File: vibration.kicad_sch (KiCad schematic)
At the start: 7 parts, among them J5 Conn_01x02, Q3 SS8050

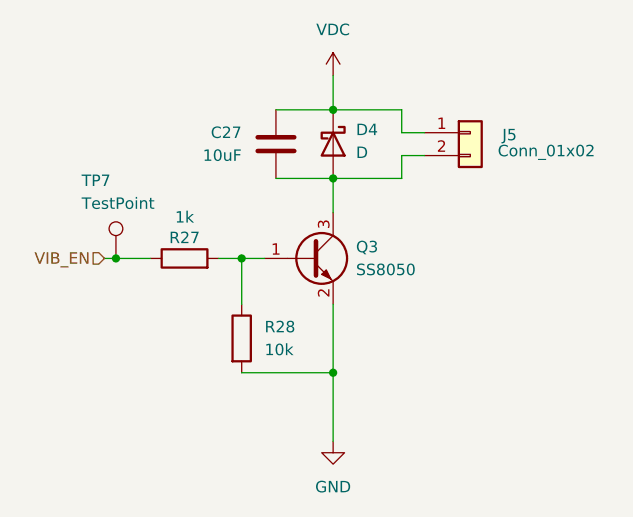
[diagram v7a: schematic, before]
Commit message: proper lcd backlight driver
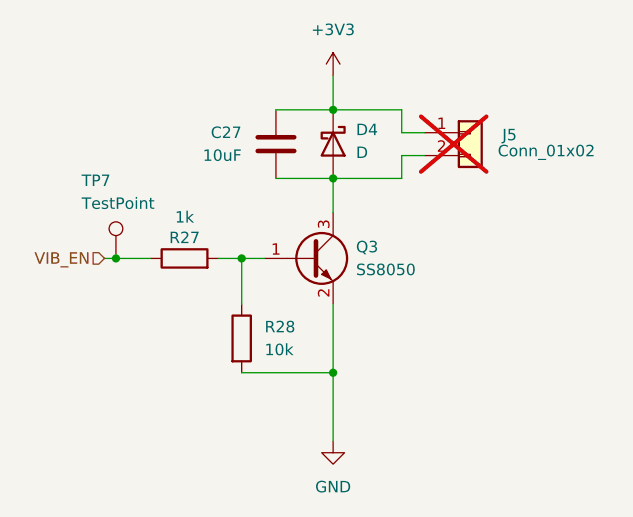
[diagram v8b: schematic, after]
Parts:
- J5: now not fitted; now left out of the parts list
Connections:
- net VDC renamed +3V3
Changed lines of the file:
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@@
+	)
+	(symbol
+		(lib_id "power:+3V3")
+		(at 132.08 67.31 0)
+		(unit 1)
+		(exclude_from_sim no)
+		(in_bom yes)
+		(on_board yes)
+		(dnp no)
+		(fields_autoplaced yes)
+		(property "Reference" "#PWR026"
+			(at 132.08 71.12 0)
+			(effects
+				(font
+					(size 1.27 1.27)
+				)
+				(hide yes)
+			)
+		)
+		(property "Value" "+3V3"
+			(at 132.08 62.23 0)
+			(effects
+				(font
+					(size 1.27 1.27)
+				)
+			)
+		)
+		(property "Footprint" ""
+			(at 132.08 67.31 0)
+			(effects
+				(font
+					(size 1.27 1.27)
+				)
+				(hide yes)
+			)
+		)
+		(property "Datasheet" ""
+			(at 132.08 67.31 0)
+			(effects
+				(font
+					(size 1.27 1.27)
+				)
+				(hide yes)
+			)
+		)
+		(property "Description" "Power symbol creates a global label with name \"+3V3\""
+			(at 132.08 67.31 0)
+			(effects
+				(font
+					(size 1.27 1.27)
+				)
+				(hide yes)
+			)
+		)
+		(pin "1"
+		)
+		(instances
+			(project ""
+				(path "/f4643692-c319-40a7-82a2-3e775c0a417f/fa61dece-89ff-456c-a30f-6bfd2f1cc11c"
+					(reference "#PWR026")
+					(unit 1)
+				)
+			)
+		)
 	)
 	(symbol
@@
 	)
 	(symbol
-		(lib_id "power:VDC")
-		(at 132.08 67.31 0)
-		(unit 1)
-		(exclude_from_sim no)
-		(in_bom yes)
-		(on_board yes)
-		(dnp no)
-		(fields_autoplaced yes)
-		(property "Reference" "#PWR026"
-			(at 132.08 71.12 0)
-			(effects
-				(font
-					(size 1.27 1.27)
-				)
-				(hide yes)
-			)
-		)
-		(property "Value" "VDC"
-			(at 132.08 62.23 0)
-			(effects
-				(font
-					(size 1.27 1.27)
-				)
-			)
-		)
-		(property "Footprint" ""
-			(at 132.08 67.31 0)
-			(effects
-				(font
-					(size 1.27 1.27)
-				)
-				(hide yes)
-			)
-		)
-		(property "Datasheet" ""
-			(at 132.08 67.31 0)
-			(effects
-				(font
-					(size 1.27 1.27)
-				)
-				(hide yes)
-			)
-		)
-		(property "Description" "Power symbol creates a global label with name \"VDC\""
-			(at 132.08 67.31 0)
-			(effects
-				(font
-					(size 1.27 1.27)
-				)
-				(hide yes)
-			)
-		)
-		(pin "1"
-		)
-		(instances
-			(project ""
-				(path "/f4643692-c319-40a7-82a2-3e775c0a417f/fa61dece-89ff-456c-a30f-6bfd2f1cc11c"
-					(reference "#PWR026")
-					(unit 1)
-				)
-			)
-		)
-	)
-	(symbol
 		(lib_id "power:GND")
 		(at 132.08 107.95 0)
@@
 		(unit 1)
 		(exclude_from_sim no)
-		(in_bom yes)
-		(on_board yes)
-		(dnp no)
+		(in_bom no)
+		(on_board yes)
+		(dnp yes)
 		(property "Reference" "J5"
 			(at 150.876 73.914 0)
